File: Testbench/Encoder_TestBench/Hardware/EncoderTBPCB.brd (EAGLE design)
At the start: 52 x 63.5 mm, 16 parts, among them IC1 7805DT, Q1 16MHz, U1 ATMEGA328P-PU, X1 C-GRID-05-15-91

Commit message: Added Print File
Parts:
- added U$1: (no value), RoboJackets-Aesthetics:ROBOBUZZ_0.6X
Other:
- board text added: "Meow"
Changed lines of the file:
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@@
 <wire x1="43.08" y1="55.87" x2="-8.89" y2="55.87" width="0" layer="20"/>
 <wire x1="-8.89" y1="55.87" x2="-8.89" y2="-7.62" width="0" layer="20"/>
+<text x="34" y="50" size="1.778" layer="1">Meow</text>
 </plain>
 <attributes>
@@
 <element name="X1" library="con-molex" package="15-91-05" value="C-GRID-05-15-91" x="-7.62" y="45.72" rot="R90"/>
 <element name="JP2" library="pinhead" package="1X16" value="" x="38.1" y="27.94" rot="R270"/>
+<element name="U$1" library="RoboJackets-Aesthetics" package="ROBOBUZZ_0.6X" value="" x="15" y="42"/>
 </elements>
 <signals>

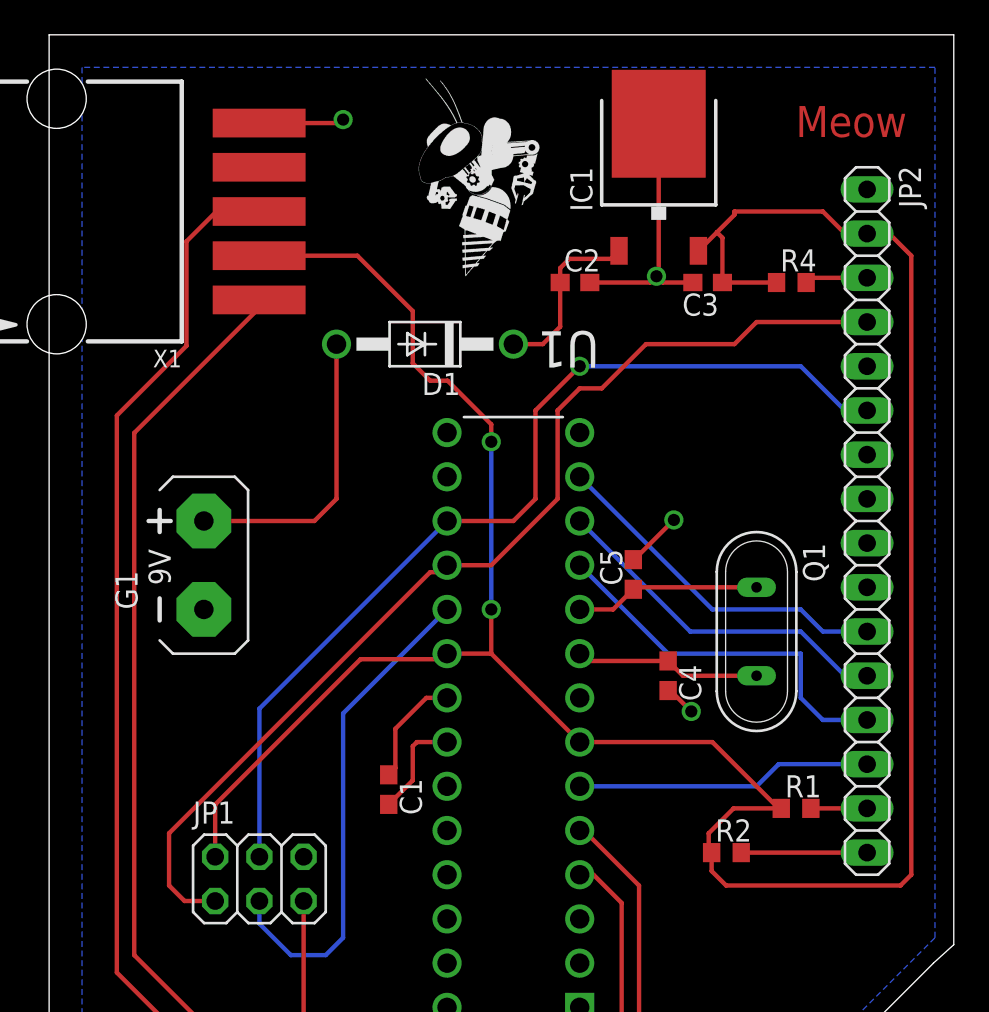
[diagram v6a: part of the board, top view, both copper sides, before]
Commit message: Unnecessary Silkscreen removed
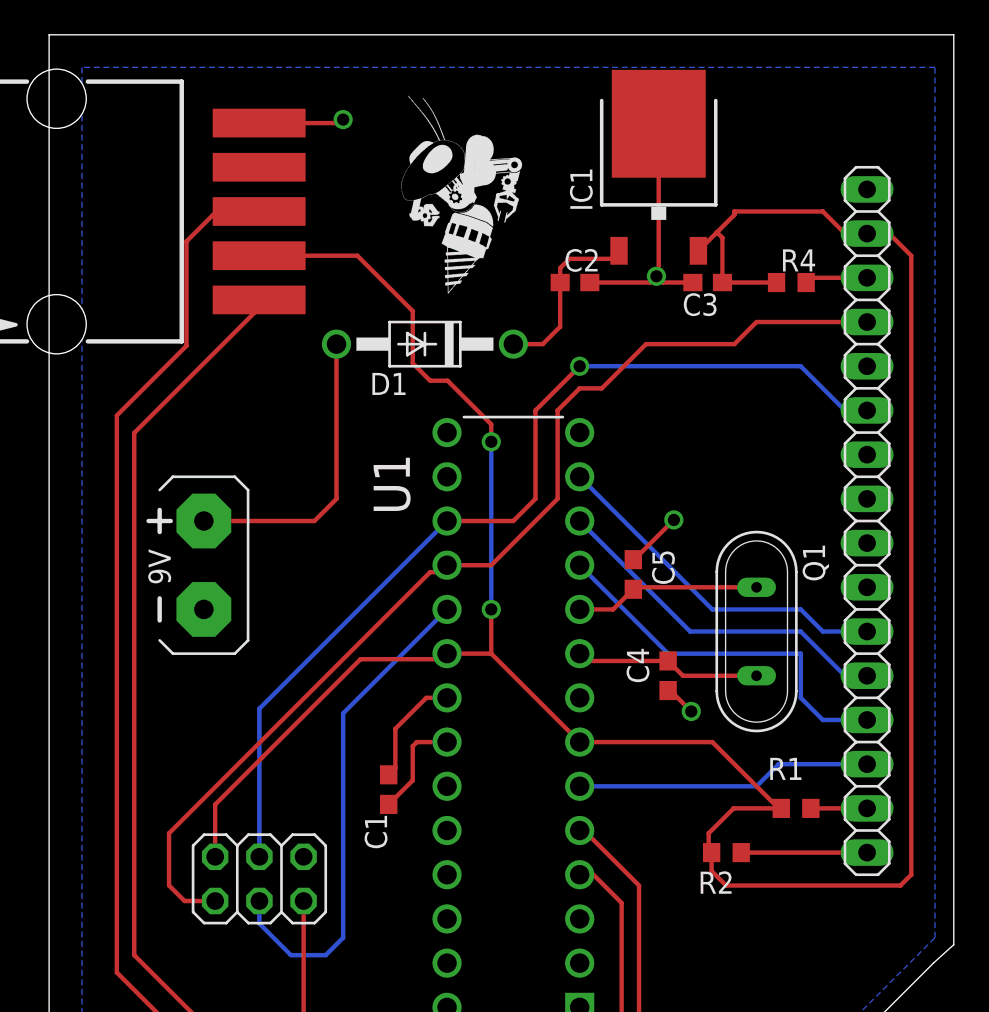
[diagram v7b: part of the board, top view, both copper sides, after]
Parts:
- moved U$1 1.41 mm to (14.0, 41.0)
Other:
- board text removed: "Meow"
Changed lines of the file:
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@@
 <layer number="27" name="tValues" color="7" fill="1" visible="yes" active="yes"/>
 <layer number="28" name="bValues" color="7" fill="1" visible="yes" active="yes"/>
-<layer number="29" name="tStop" color="7" fill="3" visible="no" active="yes"/>
-<layer number="30" name="bStop" color="7" fill="6" visible="no" active="yes"/>
-<layer number="31" name="tCream" color="7" fill="4" visible="no" active="yes"/>
-<layer number="32" name="bCream" color="7" fill="5" visible="no" active="yes"/>
-<layer number="33" name="tFinish" color="6" fill="3" visible="no" active="yes"/>
-<layer number="34" name="bFinish" color="6" fill="6" visible="no" active="yes"/>
-<layer number="35" name="tGlue" color="7" fill="4" visible="no" active="yes"/>
-<layer number="36" name="bGlue" color="7" fill="5" visible="no" active="yes"/>
-<layer number="37" name="tTest" color="7" fill="1" visible="no" active="yes"/>
-<layer number="38" name="bTest" color="7" fill="1" visible="no" active="yes"/>
+<layer number="29" name="tStop" color="7" fill="3" visible="yes" active="yes"/>
+<layer number="30" name="bStop" color="7" fill="6" visible="yes" active="yes"/>
+<layer number="31" name="tCream" color="7" fill="4" visible="yes" active="yes"/>
+<layer number="32" name="bCream" color="7" fill="5" visible="yes" active="yes"/>
+<layer number="33" name="tFinish" color="6" fill="3" visible="yes" active="yes"/>
+<layer number="34" name="bFinish" color="6" fill="6" visible="yes" active="yes"/>
+<layer number="35" name="tGlue" color="7" fill="4" visible="yes" active="yes"/>
+<layer number="36" name="bGlue" color="7" fill="5" visible="yes" active="yes"/>
+<layer number="37" name="tTest" color="7" fill="1" visible="yes" active="yes"/>
+<layer number="38" name="bTest" color="7" fill="1" visible="yes" active="yes"/>
 <layer number="39" name="tKeepout" color="4" fill="11" visible="yes" active="yes"/>
 <layer number="40" name="bKeepout" color="1" fill="11" visible="yes" active="yes"/>
@@
 <layer number="42" name="bRestrict" color="1" fill="10" visible="yes" active="yes"/>
 <layer number="43" name="vRestrict" color="2" fill="10" visible="yes" active="yes"/>
-<layer number="44" name="Drills" color="7" fill="1" visible="no" active="yes"/>
+<layer number="44" name="Drills" color="7" fill="1" visible="yes" active="yes"/>
 <layer number="45" name="Holes" color="7" fill="1" visible="yes" active="yes"/>
-<layer number="46" name="Milling" color="3" fill="1" visible="no" active="yes"/>
-<layer number="47" name="Measures" color="7" fill="1" visible="no" active="yes"/>
+<layer number="46" name="Milling" color="3" fill="1" visible="yes" active="yes"/>
+<layer number="47" name="Measures" color="7" fill="1" visible="yes" active="yes"/>
 <layer number="48" name="Document" color="7" fill="1" visible="yes" active="yes"/>
 <layer number="49" name="Reference" color="7" fill="1" visible="yes" active="yes"/>
@@
 <wire x1="43.08" y1="55.87" x2="-8.89" y2="55.87" width="0" layer="20"/>
 <wire x1="-8.89" y1="55.87" x2="-8.89" y2="-7.62" width="0" layer="20"/>
-<text x="34" y="50" size="1.778" layer="1">Meow</text>
 </plain>
 <attributes>
@@
 </autorouter>
 <elements>
-<element name="C1" library="resistor" package="C0603" value="0.1uF" x="10.62" y="12.51" rot="R270"/>
-<element name="C2" library="resistor" package="C0603" value="0.33uF" x="21.32" y="41.64"/>
-<element name="C3" library="resistor" package="C0603" value="0.1uF" x="28.94" y="41.64" rot="R180"/>
-<element name="C4" library="resistor" package="C0603" value="22pF" x="26.67" y="19.05" rot="R270"/>
-<element name="C5" library="resistor" package="C0603" value="22pF" x="24.67" y="24.87" rot="R90"/>
-<element name="D1" library="diode" package="DO41-10" value="1N4004" x="12.7" y="38.1" rot="R180"/>
-<element name="G1" library="battery" package="AB9V" value="AB9V" x="0" y="25.4"/>
+<element name="C1" library="resistor" package="C0603" value="0.1uF" x="10.62" y="12.51" smashed="yes" rot="R270">
+<attribute name="NAME" x="9.255" y="11.145" size="1.27" layer="25" rot="R270"/>
+</element>
+<element name="C2" library="resistor" package="C0603" value="0.33uF" x="21.32" y="41.64" smashed="yes">
+<attribute name="NAME" x="20.685" y="42.275" size="1.27" layer="25"/>
+</element>
+<element name="C3" library="resistor" package="C0603" value="0.1uF" x="28.94" y="41.64" smashed="yes" rot="R180">
+<attribute name="NAME" x="29.575" y="41.005" size="1.27" layer="25" rot="R180"/>
+</element>
+<element name="C4" library="resistor" package="C0603" value="22pF" x="26.67" y="19.05" smashed="yes" rot="R270">
+<attribute name="NAME" x="24.305" y="20.685" size="1.27" layer="25" rot="R270"/>
+</element>
+<element name="C5" library="resistor" package="C0603" value="22pF" x="24.67" y="24.87" smashed="yes" rot="R90">
+<attribute name="NAME" x="27.035" y="24.235" size="1.27" layer="25" rot="R90"/>
+</element>
+<element name="D1" library="diode" package="DO41-10" value="1N4004" x="12.7" y="38.1" smashed="yes" rot="R180">
+<attribute name="NAME" x="11.732" y="36.449" size="1.27" layer="25" ratio="10" rot="R180"/>
+</element>
+<element name="G1" library="battery" package="AB9V" value="AB9V" x="0" y="25.4" smashed="yes"/>
 <element name="IC1" library="linear" package="TO252" value="7805DT" x="26.13" y="48.26"/>
-<element name="JP1" library="pinhead" package="2X03" value="" x="3.19" y="7.38"/>
-<element name="Q1" library="special" package="QS" value="16MHz" x="31.75" y="21.59" rot="R270"/>
-<element name="R1" library="resistor" package="R0603" value="220" x="34.02" y="11.43"/>
-<element name="R4" library="resistor" package="R0603" value="850" x="33.75" y="41.64"/>
-<element name="U1" library="Atmel_By_element14_Batch_1-00" package="DIP254P762X457-28" value="ATMEGA328P-PU" x="13.97" y="33.02" rot="R180">
+<element name="JP1" library="pinhead" package="2X03" value="" x="3.19" y="7.38" smashed="yes">
+<attribute name="VALUE" x="-0.62" y="2.935" size="1.27" layer="27"/>
+</element>
+<element name="Q1" library="special" package="QS" value="16MHz" x="31.75" y="21.59" smashed="yes" rot="R270">
+<attribute name="NAME" x="34.417" y="26.67" size="1.27" layer="25" ratio="10" rot="R270"/>
+</element>
+<element name="R1" library="resistor" package="R0603" value="220" x="34.02" y="11.43" smashed="yes">
+<attribute name="NAME" x="32.385" y="13.065" size="1.27" layer="25"/>
+</element>
+<element name="R4" library="resistor" package="R0603" value="850" x="33.75" y="41.64" smashed="yes">
+<attribute name="NAME" x="33.115" y="42.275" size="1.27" layer="25"/>
+</element>
+<element name="U1" library="Atmel_By_element14_Batch_1-00" package="DIP254P762X457-28" value="ATMEGA328P-PU" x="13.97" y="33.02" smashed="yes" rot="R180">
 <attribute name="OC_FARNELL" value="1715487" x="13.97" y="33.02" size="1.778" layer="27" rot="R180" display="off"/>
 <attribute name="OC_NEWARK" value="15R0268" x="13.97" y="33.02" size="1.778" layer="27" rot="R180" display="off"/>
@@
 <attribute name="MPN" value="ATMEGA328P-PU" x="13.97" y="33.02" size="1.778" layer="27" rot="R180" display="off"/>
 <attribute name="SUPPLIER" value="Atmel" x="13.97" y="33.02" size="1.778" layer="27" rot="R180" display="off"/>
-</element>
-<element name="R2" library="resistor" package="R0603" value="200" x="30.02" y="8.89"/>
-<element name="X1" library="con-molex" package="15-91-05" value="C-GRID-05-15-91" x="-7.62" y="45.72" rot="R90"/>
-<element name="JP2" library="pinhead" package="1X16" value="" x="38.1" y="27.94" rot="R270"/>
-<element name="U$1" library="RoboJackets-Aesthetics" package="ROBOBUZZ_0.6X" value="" x="15" y="42"/>
+<attribute name="NAME" x="11.8366" y="28.2924" size="2.0828" layer="25" ratio="10" rot="SR90"/>
+</element>
+<element name="R2" library="resistor" package="R0603" value="200" x="30.02" y="8.89" smashed="yes">
+<attribute name="NAME" x="28.385" y="6.525" size="1.27" layer="25"/>
+</element>
+<element name="X1" library="con-molex" package="15-91-05" value="C-GRID-05-15-91" x="-7.62" y="45.72" smashed="yes" rot="R90">
+<attribute name="VALUE" x="1.27" y="53.0725" size="0.8128" layer="27" ratio="10"/>
+</element>
+<element name="JP2" library="pinhead" package="1X16" value="" x="38.1" y="27.94" smashed="yes" rot="R270">
+<attribute name="VALUE" x="34.925" y="48.26" size="1.27" layer="27" rot="R270"/>
+</element>
+<element name="U$1" library="RoboJackets-Aesthetics" package="ROBOBUZZ_0.6X" value="" x="14" y="41"/>
 </elements>
 <signals>

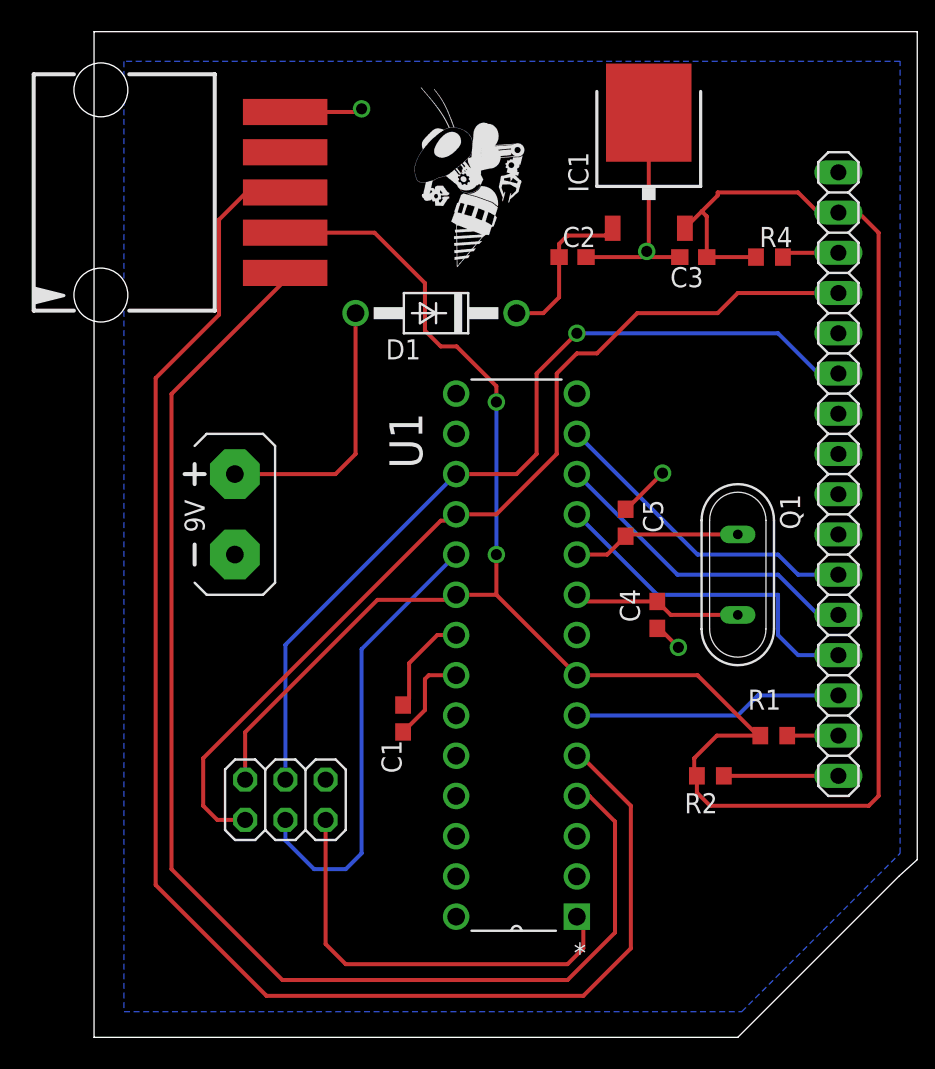
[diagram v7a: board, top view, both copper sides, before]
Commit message: Serial Communication Connector Added
Thanks @2Ryan09 for pointing that out.
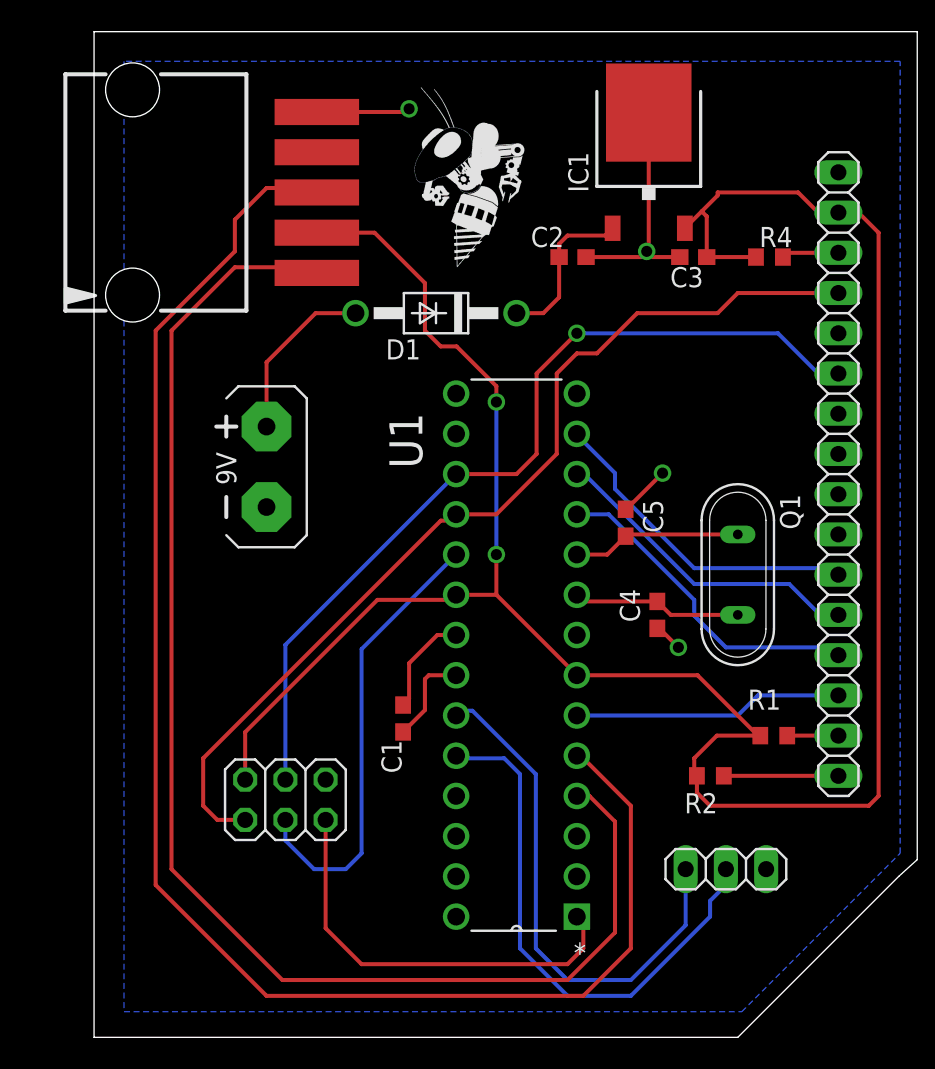
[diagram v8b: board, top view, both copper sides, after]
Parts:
- added JP3: (no value), pinhead:1X03
- moved G1 3.61 mm to (2.00, 28.4)
- moved X1 2.00 mm to (-5.62, 45.7)
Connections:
- new net RX: JP3.1, U1.23
- new net TX: JP3.2, U1.24
- net GND: now also JP3.3
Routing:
- net TX: track 0.00 -> 34.2 mm
- net RX: track 0.00 -> 33.1 mm
- net ENPA: track 82.8 -> 89.3 mm
- net N$15: track 17.0 -> 11.9 mm
- net ENPB: track 96.6 -> 99.1 mm
- net VDD: track 150.2 -> 148.2 mm
- net GND: track 39.7 -> 40.7 mm
- net P5T13: track 21.7 -> 20.8 mm
- net P7T11: track 20.2 -> 20.8 mm
- net PC6: track 27.2 -> 26.6 mm
